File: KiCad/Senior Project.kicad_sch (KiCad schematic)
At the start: 29 parts, among them J1 USB_C_Receptacle_USB2.0_16P, J2 Screw_Terminal_01x02, J3 Screw_Terminal_01x06, SW1 SW_Push, SW2 SW_Push, U1 ESP32-S3FH4R2, X1 FC-135 32.7680KA-A5, Y2 Crystal_GND23

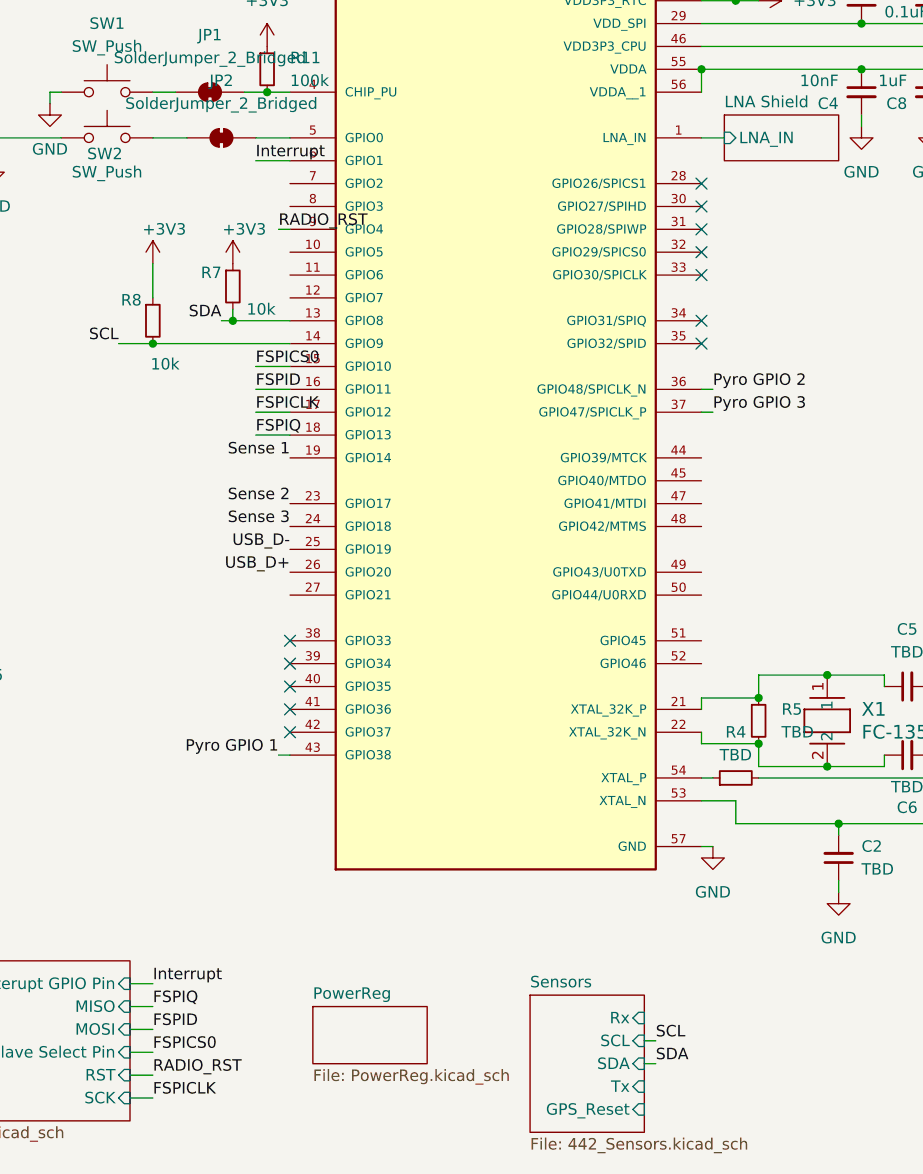
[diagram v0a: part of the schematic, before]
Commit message: ERC fixes
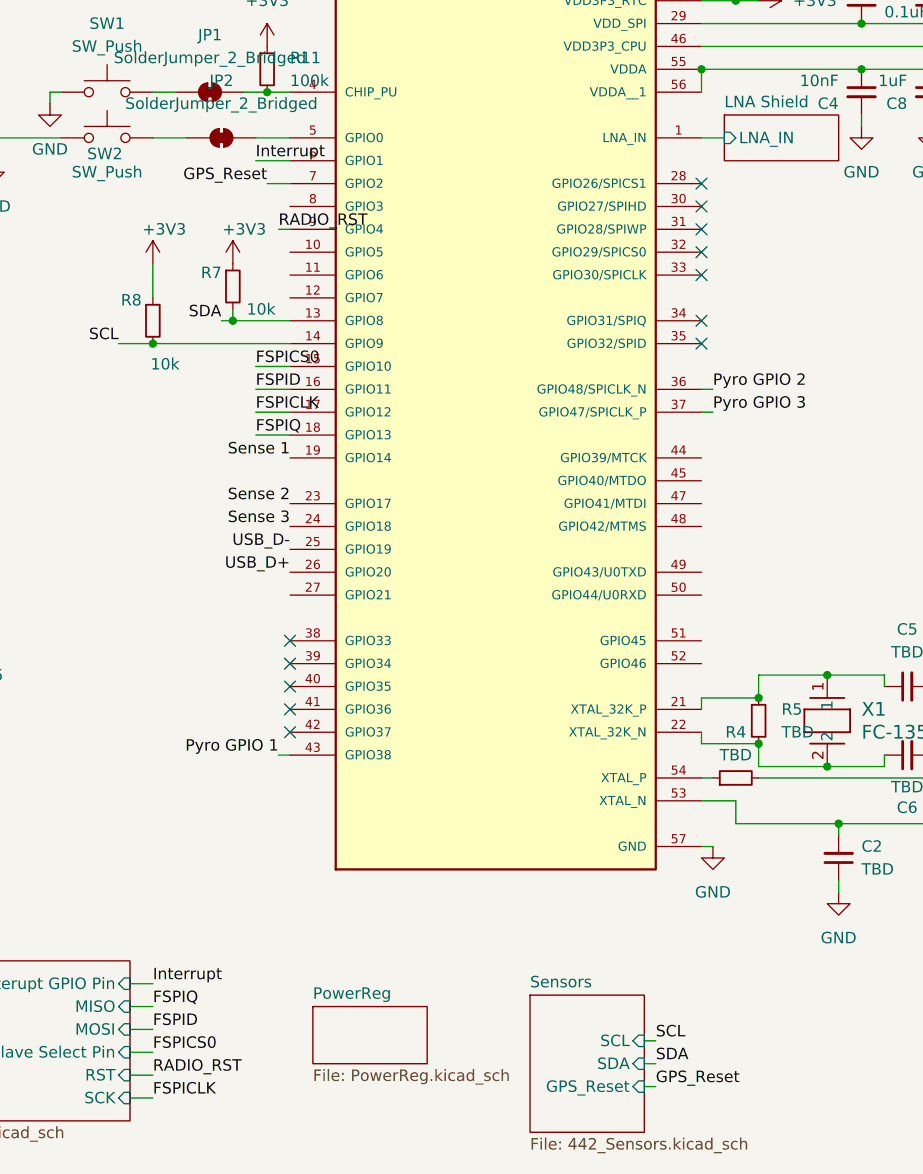
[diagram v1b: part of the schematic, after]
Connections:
- net GPS_Reset: now reaches U1.7 (GPIO2)
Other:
- sheet Sensors ports: added none; removed Rx, Tx
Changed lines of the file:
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@@
 	(wire
 		(pts
+			(xy 160.02 172.72) (xy 161.29 172.72)
+		)
+		(stroke
+			(width 0)
+			(type default)
+		)
+	)
+	(wire
+		(pts
 			(xy 119.38 135.89) (xy 120.65 135.89)
 		)
@@
 	(wire
 		(pts
+			(xy 118.11 72.39) (xy 120.65 72.39)
+		)
+		(stroke
+			(width 0)
+			(type default)
+		)
+	)
+	(wire
+		(pts
 			(xy 191.77 66.04) (xy 191.77 64.77)
 		)
@@
 		)
 	)
+	(label "GPS_Reset"
+		(at 118.11 72.39 180)
+		(effects
+			(font
+				(size 1.27 1.27)
+			)
+			(justify right bottom)
+		)
+	)
 	(label "Interrupt"
 		(at 105.41 161.29 0)
@@
 		)
 	)
+	(label "GPS_Reset"
+		(at 161.29 172.72 0)
+		(effects
+			(font
+				(size 1.27 1.27)
+			)
+			(justify left bottom)
+		)
+	)
 	(label "Pyro GPIO 1"
 		(at 119.38 135.89 180)
@@
 			)
 		)
-		(pin "Rx" input
-			(at 160.02 165.1 0)
-			(effects
-				(font
-					(size 1.27 1.27)
-				)
-				(justify right)
-			)
-		)
 		(pin "SCL" input
 			(at 160.02 167.64 0)
@@
 			)
 		)
-		(pin "Tx" input
-			(at 160.02 172.72 0)
-			(effects
-				(font
-					(size 1.27 1.27)
-				)
-				(justify right)
-			)
-		)
 		(pin "GPS_Reset" input
-			(at 160.02 175.26 0)
+			(at 160.02 172.72 0)
 			(effects
 				(font
